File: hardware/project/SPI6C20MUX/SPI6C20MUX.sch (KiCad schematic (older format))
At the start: 4 parts

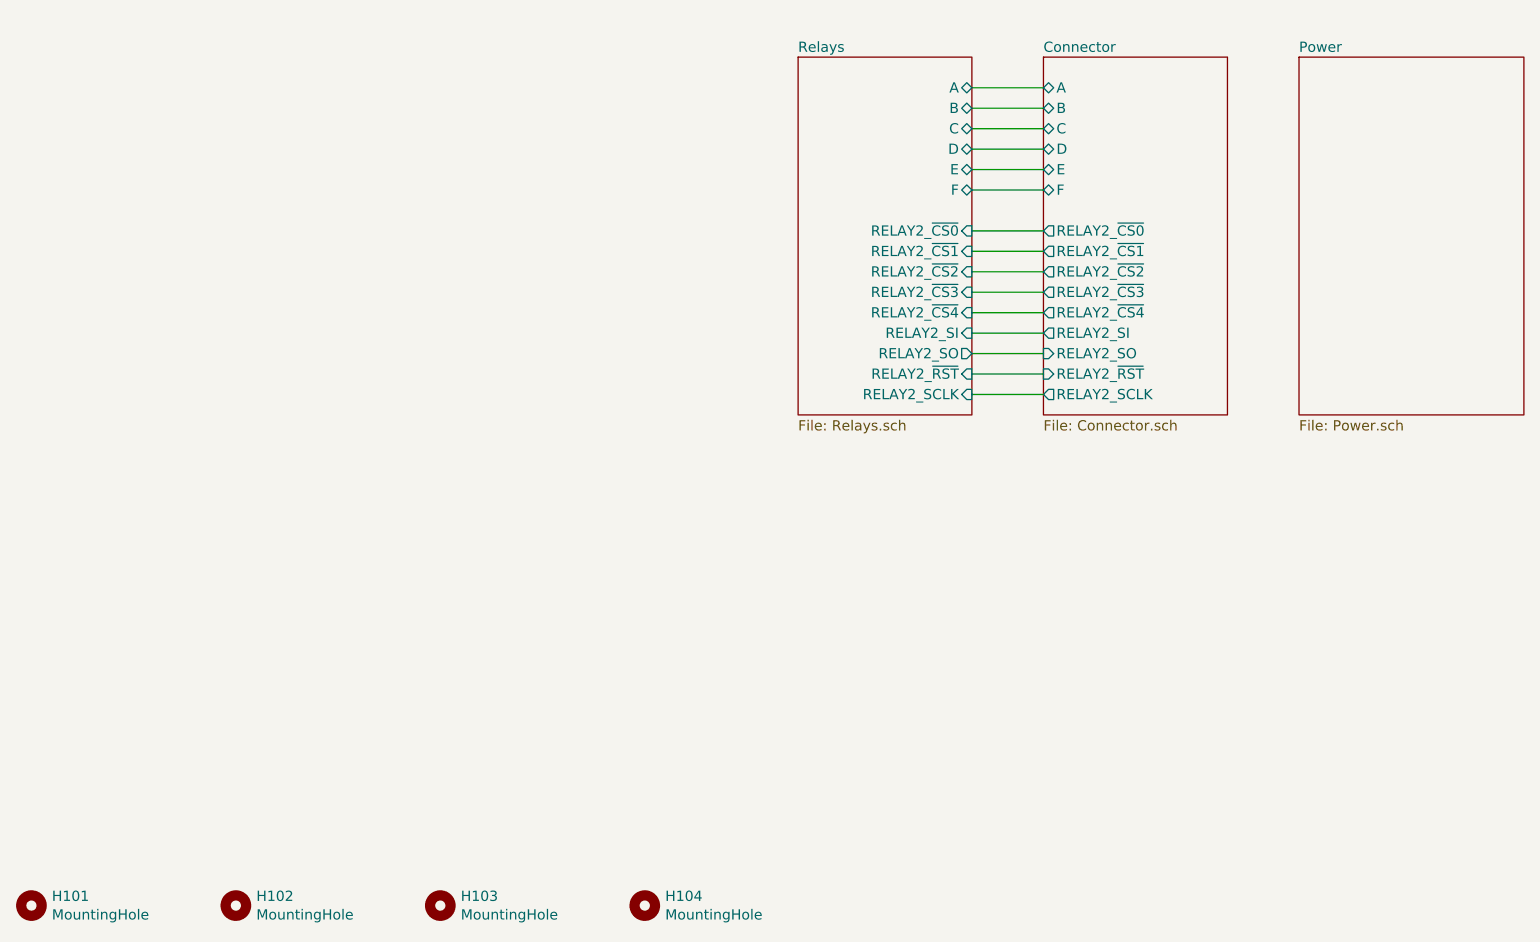
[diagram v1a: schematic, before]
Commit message: PCB main and module layout.
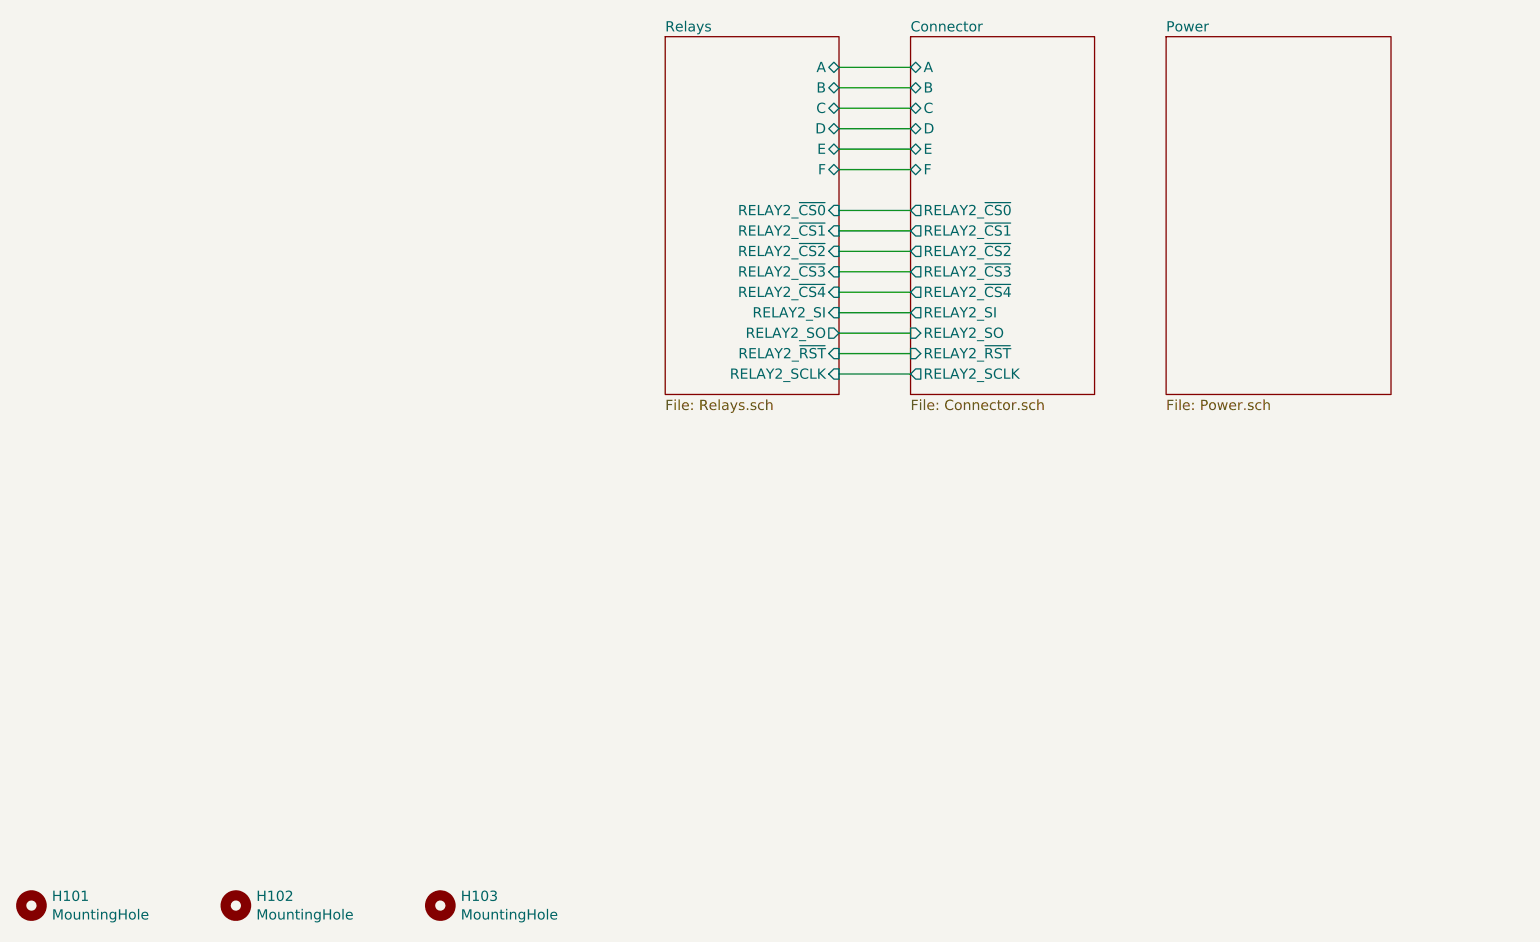
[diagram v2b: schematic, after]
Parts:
- removed H104: MountingHole, MountingHole:MountingHole_3.2mm_M3_DIN965_Pad, symbol Mechanical:MountingHole
- H101, H102, H103: footprint MountingHole:MountingHole_3.2mm_M3_DIN965_Pad -> MountingHole:MountingHole_2.7mm_M2.5_DIN965_Pad
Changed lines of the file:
@@
 $EndDescr
 $Sheet
-S 4750 2850 850  1750
+S 4100 2750 850  1750
 U 5D94E82E
 F0 "Relays" 50
 F1 "Relays.sch" 50
-F2 "F" B R 5600 3500 50
-F3 "B" B R 5600 3100 50
-F4 "E" B R 5600 3400 50
-F5 "C" B R 5600 3200 50
-F6 "D" B R 5600 3300 50
-F7 "RELAY2_~CS0" I R 5600 3700 50
-F8 "RELAY2_~CS1" I R 5600 3800 50
-F9 "RELAY2_~CS2" I R 5600 3900 50
-F10 "RELAY2_~CS3" I R 5600 4000 50
-F11 "RELAY2_SCLK" I R 5600 4500 50
-F12 "RELAY2_SI" I R 5600 4200 50
-F13 "RELAY2_SO" O R 5600 4300 50
-F14 "RELAY2_~RST" I R 5600 4400 50
-F15 "A" B R 5600 3000 50
-F16 "RELAY2_~CS4" I R 5600 4100 50
+F2 "F" B R 4950 3400 50
+F3 "B" B R 4950 3000 50
+F4 "E" B R 4950 3300 50
+F5 "C" B R 4950 3100 50
+F6 "D" B R 4950 3200 50
+F7 "RELAY2_~CS0" I R 4950 3600 50
+F8 "RELAY2_~CS1" I R 4950 3700 50
+F9 "RELAY2_~CS2" I R 4950 3800 50
+F10 "RELAY2_~CS3" I R 4950 3900 50
+F11 "RELAY2_SCLK" I R 4950 4400 50
+F12 "RELAY2_SI" I R 4950 4100 50
+F13 "RELAY2_SO" O R 4950 4200 50
+F14 "RELAY2_~RST" I R 4950 4300 50
+F15 "A" B R 4950 2900 50
+F16 "RELAY2_~CS4" I R 4950 4000 50
 $EndSheet
 $Sheet
-S 5950 2850 900  1750
+S 5300 2750 900  1750
 U 5DAAD438
 F0 "Connector" 50
 F1 "Connector.sch" 50
-F2 "A" B L 5950 3000 50
-F3 "B" B L 5950 3100 50
-F4 "C" B L 5950 3200 50
-F5 "D" B L 5950 3300 50
-F6 "E" B L 5950 3400 50
-F7 "F" B L 5950 3500 50
-F8 "RELAY2_~CS2" O L 5950 3900 50
-F9 "RELAY2_~CS1" O L 5950 3800 50
-F10 "RELAY2_~CS0" O L 5950 3700 50
-F11 "RELAY2_SCLK" O L 5950 4500 50
-F12 "RELAY2_SI" O L 5950 4200 50
-F13 "RELAY2_SO" I L 5950 4300 50
-F14 "RELAY2_~RST" I L 5950 4400 50
-F15 "RELAY2_~CS3" O L 5950 4000 50
-F16 "RELAY2_~CS4" O L 5950 4100 50
+F2 "A" B L 5300 2900 50
+F3 "B" B L 5300 3000 50
+F4 "C" B L 5300 3100 50
+F5 "D" B L 5300 3200 50
+F6 "E" B L 5300 3300 50
+F7 "F" B L 5300 3400 50
+F8 "RELAY2_~CS2" O L 5300 3800 50
+F9 "RELAY2_~CS1" O L 5300 3700 50
+F10 "RELAY2_~CS0" O L 5300 3600 50
+F11 "RELAY2_SCLK" O L 5300 4400 50
+F12 "RELAY2_SI" O L 5300 4100 50
+F13 "RELAY2_SO" I L 5300 4200 50
+F14 "RELAY2_~RST" I L 5300 4300 50
+F15 "RELAY2_~CS3" O L 5300 3900 50
+F16 "RELAY2_~CS4" O L 5300 4000 50
 $EndSheet
 Wire Wire Line
-	5600 3000 5950 3000
+	4950 2900 5300 2900
 Wire Wire Line
-	5950 3100 5600 3100
+	5300 3000 4950 3000
 Wire Wire Line
-	5600 3200 5950 3200
+	4950 3100 5300 3100
 Wire Wire Line
-	5950 3300 5600 3300
+	5300 3200 4950 3200
 Wire Wire Line
-	5600 3400 5950 3400
+	4950 3300 5300 3300
 Wire Wire Line
-	5950 3500 5600 3500
+	5300 3400 4950 3400
 Wire Wire Line
-	5600 3700 5950 3700
+	4950 3600 5300 3600
 Wire Wire Line
-	5950 3800 5600 3800
+	5300 3700 4950 3700
 Wire Wire Line
-	5600 3900 5950 3900
+	4950 3800 5300 3800
 Wire Wire Line
-	5950 4000 5600 4000
+	5300 3900 4950 3900
 Wire Wire Line
-	5600 4100 5950 4100
+	4950 4000 5300 4000
 Wire Wire Line
-	5950 4200 5600 4200
+	5300 4100 4950 4100
 Wire Wire Line
-	5600 4300 5950 4300
+	4950 4200 5300 4200
 Wire Wire Line
-	5950 4400 5600 4400
+	5300 4300 4950 4300
 Wire Wire Line
-	5600 4500 5950 4500
+	4950 4400 5300 4400
 $Comp
 L Mechanical:MountingHole H101
@@
 F 0 "H101" H 1100 7046 50  0000 L CNN
 F 1 "MountingHole" H 1100 6955 50  0000 L CNN
-F 2 "MountingHole:MountingHole_3.2mm_M3_DIN965_Pad" H 1000 7000 50  0001 C CNN
+F 2 "MountingHole:MountingHole_2.7mm_M2.5_DIN965_Pad" H 1000 7000 50  0001 C CNN
 F 3 "~" H 1000 7000 50  0001 C CNN
 	1    1000 7000
@@
 F 0 "H102" H 2100 7046 50  0000 L CNN
 F 1 "MountingHole" H 2100 6955 50  0000 L CNN
-F 2 "MountingHole:MountingHole_3.2mm_M3_DIN965_Pad" H 2000 7000 50  0001 C CNN
+F 2 "MountingHole:MountingHole_2.7mm_M2.5_DIN965_Pad" H 2000 7000 50  0001 C CNN
 F 3 "~" H 2000 7000 50  0001 C CNN
 	1    2000 7000
@@
 F 0 "H103" H 3100 7046 50  0000 L CNN
 F 1 "MountingHole" H 3100 6955 50  0000 L CNN
-F 2 "MountingHole:MountingHole_3.2mm_M3_DIN965_Pad" H 3000 7000 50  0001 C CNN
+F 2 "MountingHole:MountingHole_2.7mm_M2.5_DIN965_Pad" H 3000 7000 50  0001 C CNN
 F 3 "~" H 3000 7000 50  0001 C CNN
 	1    3000 7000
 	1    0    0    -1
 $EndComp
-$Comp
-L Mechanical:MountingHole H104
-U 1 1 5DACE154
-P 4000 7000
-F 0 "H104" H 4100 7046 50  0000 L CNN
-F 1 "MountingHole" H 4100 6955 50  0000 L CNN
-F 2 "MountingHole:MountingHole_3.2mm_M3_DIN965_Pad" H 4000 7000 50  0001 C CNN
-F 3 "~" H 4000 7000 50  0001 C CNN
-	1    4000 7000
-	1    0    0    -1
-$EndComp
 $Sheet
-S 7200 2850 1100 1750
+S 6550 2750 1100 1750
 U 5DDB03BB
 F0 "Power" 50
